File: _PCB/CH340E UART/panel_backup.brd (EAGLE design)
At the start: 21.1 x 11.4 mm, 11 parts, among them IC1 REG1117

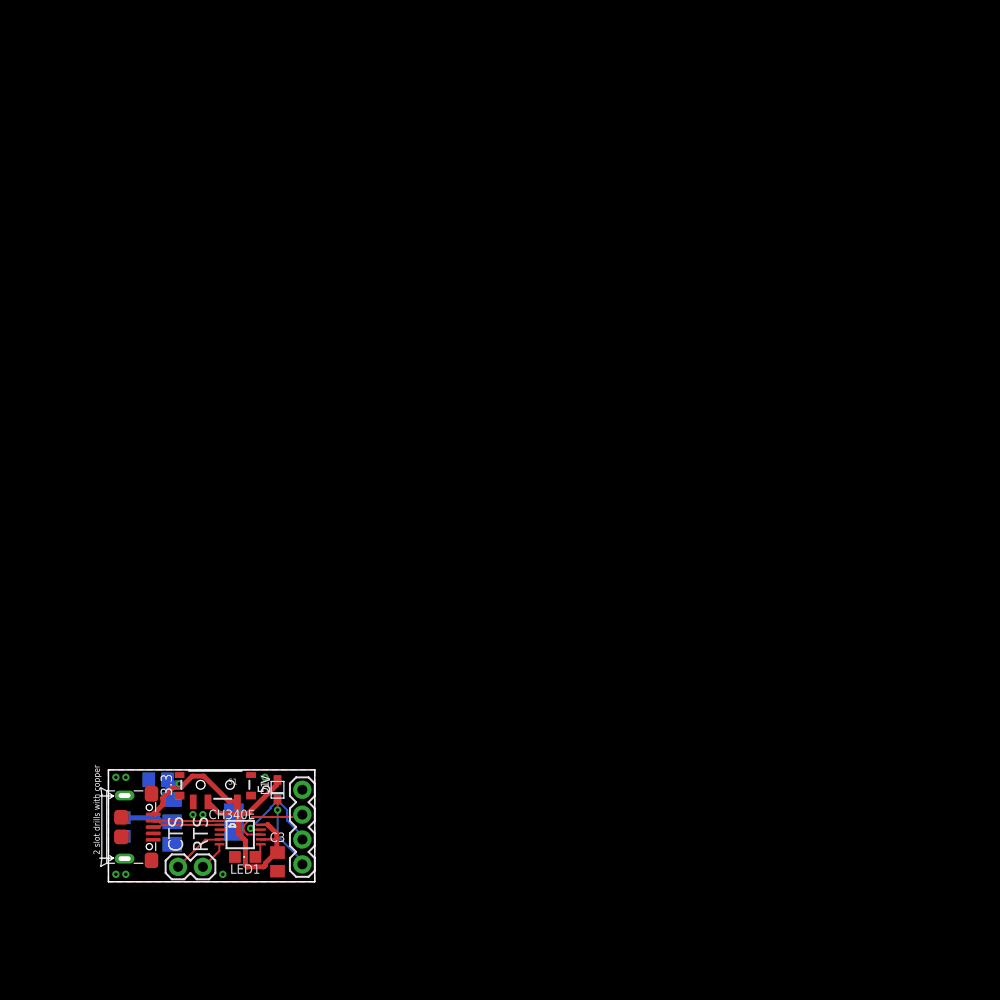
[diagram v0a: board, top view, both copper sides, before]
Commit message: CH340E board panelized
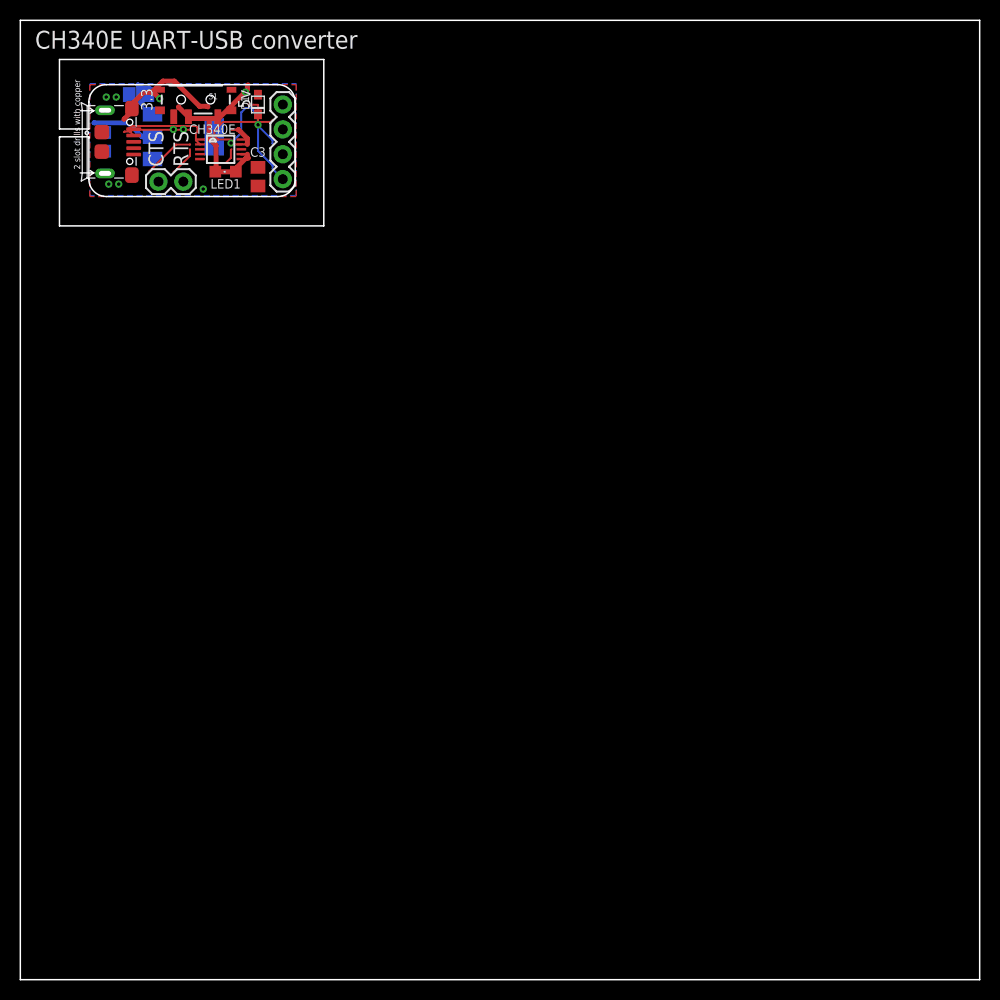
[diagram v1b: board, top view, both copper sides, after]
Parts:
- moved C1 70.0 mm to (3.08, 80.4)
- moved C2 70.0 mm to (-0.48, 75.6)
- moved C3 70.0 mm to (15.3, 72.0)
- moved CH340E 70.0 mm to (11.5, 74.8)
- moved D1 70.0 mm to (15.3, 79.4)
- moved IC1 70.0 mm to (7.65, 76.1)
- moved J1 70.0 mm to (17.8, 71.8)
- moved J2 70.0 mm to (7.65, 71.5)
- moved LED1 70.0 mm to (12.0, 72.5)
- moved S1 70.0 mm to (8.92, 79.9)
- moved USB2 70.0 mm to (2.83, 75.6)
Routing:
- net VCC: track 24.4 -> 22.4 mm
- net VCC_D: track 7.68 -> 9.64 mm
- net 3V3: track 5.15 -> 6.56 mm
- net USBN: track 9.02 -> 10.2 mm
- net 5V: track 15.7 -> 16.4 mm
- net RX: track 9.90 -> 10.5 mm
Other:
- board size 21.1 x 11.4 mm -> 98 x 98 mm
- board text added: "CH340E UART-USB converter"
